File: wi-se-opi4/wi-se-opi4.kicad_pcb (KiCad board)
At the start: 4 copper layers, 17 x 26.5 mm, 34 parts, among them J1 UART, J2 Side, Q1 SS8050-G, Q2 SS8050-G, SW1 RESET, SW2 BOOT0, U1 AMS1117-3.3, U2 ESP-WROOM-02

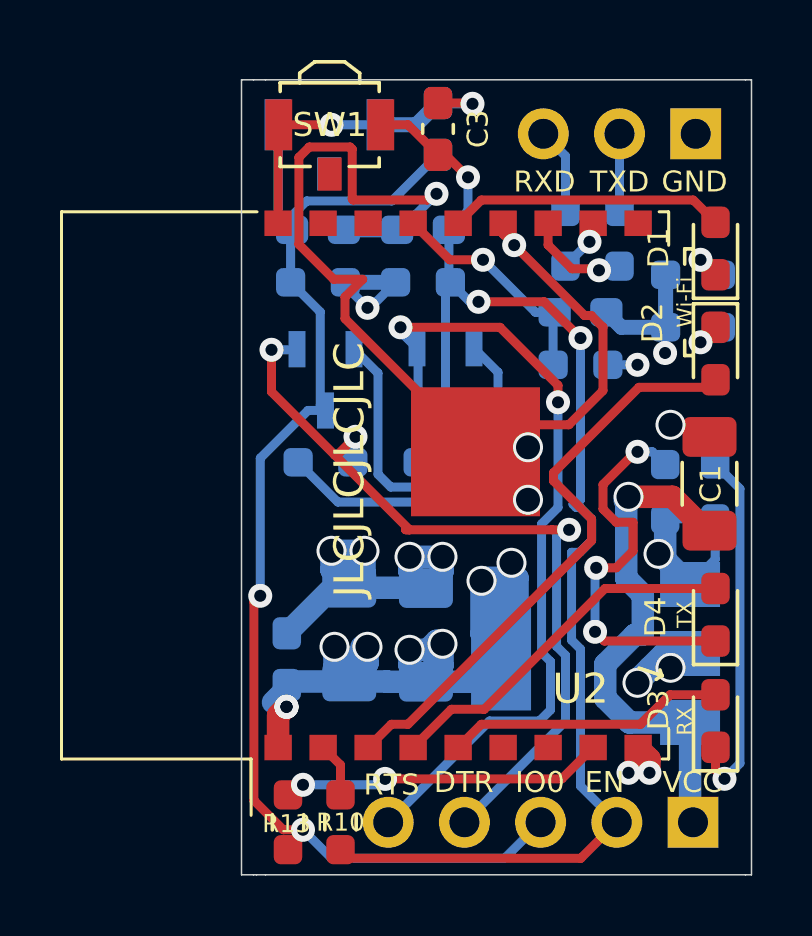
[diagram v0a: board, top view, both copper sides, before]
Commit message: Update Opi4 version
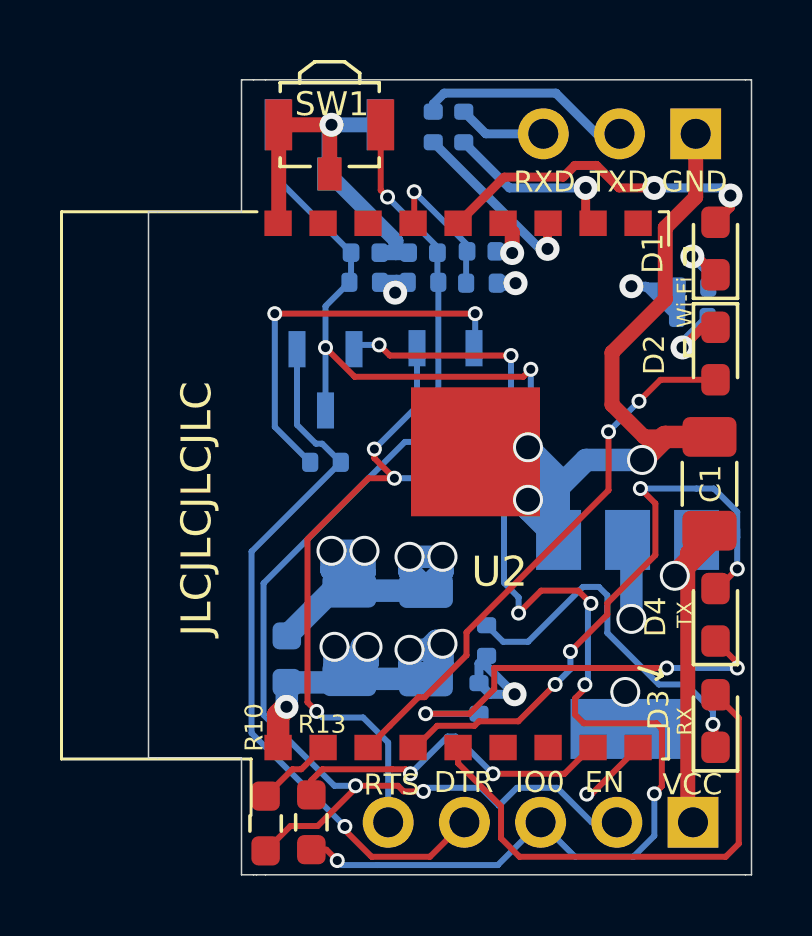
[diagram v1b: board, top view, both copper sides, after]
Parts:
- removed C3, C4: 0u1, Capacitor_SMD:C_0603_1608Metric_Pad1.08x0.95mm_HandSolder
- added REF**: oshw, wi-se:oshw, B.Cu at (110.2, 77.9)
- C1: value 22u -> 10u
- C2, C5: value 22u -> 10u; footprint Capacitor_SMD:C_1206_3216Metric_Pad1.33x1.80mm_HandSolder -> Capacitor_SMD:C_1206_3216Metric
- C6: footprint Capacitor_SMD:C_0603_1608Metric_Pad1.08x0.95mm_HandSolder -> Capacitor_SMD:C_0603_1608Metric
- C7, C8, C9: footprint Capacitor_SMD:C_0603_1608Metric_Pad1.08x0.95mm_HandSolder -> Capacitor_SMD:C_0402_1005Metric
- R1, R2, R3, R4, R5, R6, R7, R8, R9: footprint Resistor_SMD:R_0603_1608Metric_Pad0.98x0.95mm_HandSolder -> Resistor_SMD:R_0402_1005Metric
- R10, R13: value 0 -> 1k
- R11, R12: value 0 -> 1k; footprint Resistor_SMD:R_0603_1608Metric_Pad0.98x0.95mm_HandSolder -> Resistor_SMD:R_0402_1005Metric
- moved R4 9.27 mm to (102.6, 87.1), turned to 270 degrees
- moved R3 9.10 mm to (102.9, 85.2)
- moved R12 7.24 mm to (101.1, 68.1)
- moved R11 5.04 mm to (102.1, 68.1)
- moved R7 4.28 mm to (102.7, 73.3)
- moved C9 3.88 mm to (102.7, 72.2)
- moved R10 2.50 mm to (95.5, 91.3)
- moved C7 1.76 mm to (98.8, 72.3)
- moved R5 1.56 mm to (98.8, 73.2)
- moved U1 1.24 mm to (107.6, 85.0), turned to 270 degrees
- moved R13 0.78 mm to (97.0, 91.2)
- moved C8 0.76 mm to (100.8, 72.3)
- moved R1 0.41 mm to (109.8, 73.4)
- moved R2 0.33 mm to (109.7, 74.4)
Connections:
- SW1 pad 3: (no net) -> GND
- SW2 pad 3: (no net) -> GND
- U2 pad 10: Net-(U2-Pad10) -> (no net)
- U2 pad 16: Net-(U2-Pad16) -> (no net)
- U2 pad 17: Net-(U2-Pad17) -> (no net)
- U2 pad 6: Net-(U2-Pad6) -> (no net)
- U2 pad 7: Net-(U2-Pad7) -> (no net)
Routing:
- net +3V3: track 43.0 -> 23.9 mm, vias 12 -> 9
- net BOOT0: track 42.6 -> 53.5 mm, vias 2 -> 7
- net LED_RX: track 12.3 -> 20.5 mm, vias 0 -> 4
- net LED_TX: track 9.31 -> 17.3 mm
- net RTS: track 28.9 -> 21.7 mm, vias 2 -> 3
- net TXD: track 2.59 -> 7.17 mm
- net Net-(R11-Pad1): track 1.81 -> 5.97 mm
- net VCC: track 17.4 -> 13.6 mm
- net DTR: track 27.7 -> 24.1 mm, vias 3 -> 1
- net EN: track 44.9 -> 41.6 mm
- net RST: track 7.72 -> 4.86 mm
- net Net-(R12-Pad1): track 3.47 -> 6.14 mm
- net LED_WIFI: track 9.21 -> 11.4 mm, vias 0 -> 2
- net LED_STATUS: track 19.8 -> 18.2 mm, vias 0 -> 2
- net Net-(Q2-Pad2): track 8.18 -> 9.69 mm, vias 0 -> 2
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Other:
- board size 17 x 26.5 mm -> 20.1 x 26.5 mm
- board text added: "CERN-OHL-S"

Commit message: Replace buttons with cheap aliexpress ones
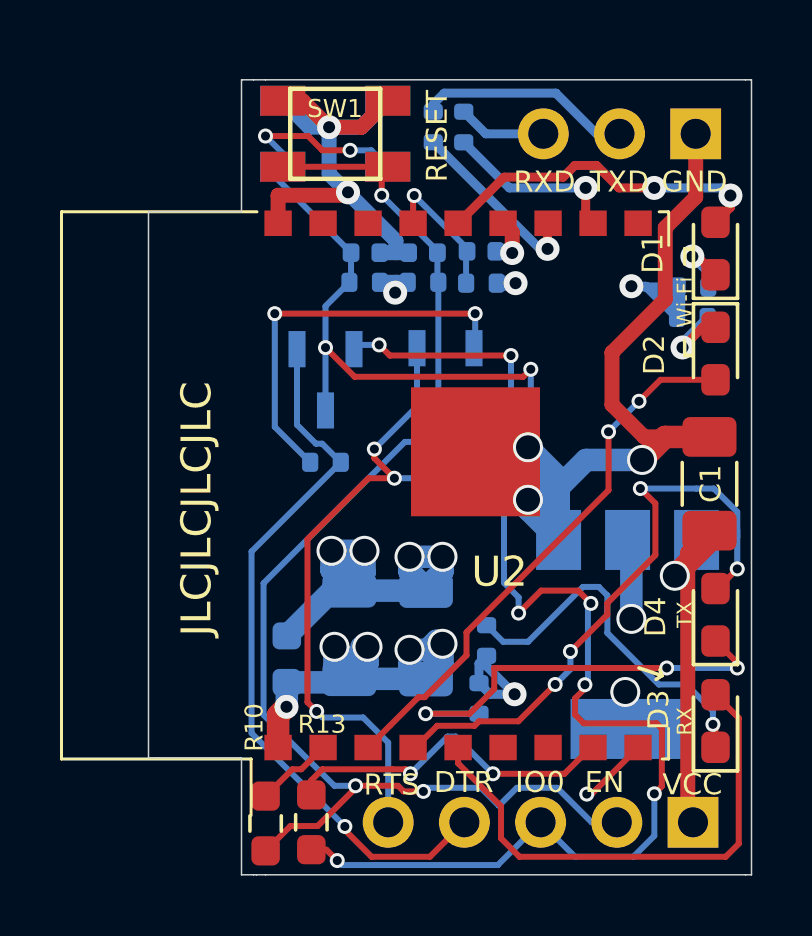
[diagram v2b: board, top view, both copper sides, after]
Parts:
- SW1, SW2: footprint Button_Switch_SMD:SW_SPST_B3U-3100P -> aliexpress-switch:Tactile_Push_Button_SMD_3x3x1.5mm.kicad_mod
- moved REF** 19.0 mm to (93.9, 87.5)
- moved SW2 0.56 mm to (97.8, 68.3)
- moved SW1 0.55 mm to (97.8, 68.3)
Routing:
- net BOOT0: track 53.5 -> 57.5 mm, vias 7 -> 9
- net GND: track 76.5 -> 79.9 mm, vias 12 -> 13
- net EN: track 41.6 -> 44.0 mm
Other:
- board text added: "BOOT0"
- board text added: "RESET"

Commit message: opi4: Add missing GPIO15 pull-down
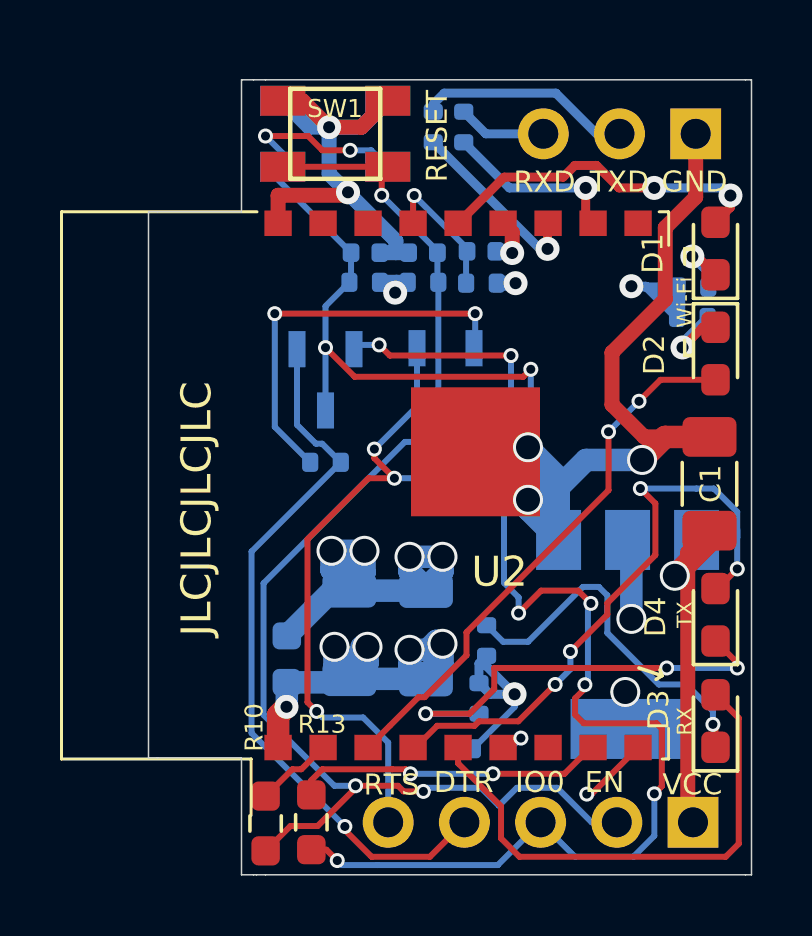
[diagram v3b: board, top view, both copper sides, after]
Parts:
- removed REF**: oshw, wi-se:oshw
- added R14: 10k, Resistor_SMD:R_0402_1005Metric, B.Cu at (102.9, 88.8)
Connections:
- U2 pad 6: (no net) -> Net-(R14-Pad1)
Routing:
- net GND: track 79.9 -> 82.3 mm
- net Net-(R14-Pad1): track 0.00 -> 1.45 mm, vias 0 -> 1
- net Net-(R13-Pad2): track 11.5 -> 10.5 mm

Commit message: Update version numbers on all documents
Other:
- board text added: "for opi4 v0.2"
- board text removed: "for opi4 v0.1"
